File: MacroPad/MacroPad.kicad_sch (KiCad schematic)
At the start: 26 parts, among them SW1 CherryMX, SW10 CherryMX, SW12 CherryMX, SW2 CherryMX, SW3 CherryMX, SW4 CherryMX, SW5 CherryMX, SW6 CherryMX, SW7 CherryMX, SW8 CherryMX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

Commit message: updated materials list
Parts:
- added O1: SSD1306, Connector_PinSocket_2.54mm:PinSocket_1x04_P2.54mm_Vertical, symbol Connector:Conn_01x04_Male
- added SW11: CherryMX, Switch_Keyboard_Cherry_MX:SW_Cherry_MX_Plate_1.00u, symbol CherryMX:CherryMX
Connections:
- net GND: now also O1.4 (Pin_4), SW11.2
- net SW1: now also U1.25 (*GPIO0/BOOT/ADC2_CH1); no longer U1.7 (32K_XP/GPIO32/ADC1_CH4)
- net SW10: now also U1.28 (GPIO17); no longer U1.10 (DAC_2/ADC2_CH9/GPIO26)
- net SW11: now also U1.29 (*GPIO5), SW11.1; no longer U1.11 (ADC2_CH7/GPIO27)
- net SW12: now also U1.12 (MTMS/GPIO14/ADC2_CH6); no longer U1.36 (GPIO22)
- net SW2: now also U1.13 (*MTDI/GPIO12/ADC2_CH5); no longer U1.37 (GPIO23)
- net SW3: now also U1.9 (DAC_1/ADC2_CH8/GPIO25); no longer U1.30 (GPIO18)
- net SW4: now also U1.26 (ADC2_CH0/GPIO4); no longer U1.8 (32K_XN/GPIO33/ADC1_CH5)
- net SW5: now also U1.31 (GPIO19); no longer U1.13 (*MTDI/GPIO12/ADC2_CH5)
- net SW6: now also U1.10 (DAC_2/ADC2_CH9/GPIO26); no longer U1.31 (GPIO19)
- net SW7: now also U1.27 (GPIO16); no longer U1.9 (DAC_1/ADC2_CH8/GPIO25)
- net SW8: now also U1.30 (GPIO18); no longer U1.12 (MTMS/GPIO14/ADC2_CH6)
- net SW9: now also U1.11 (ADC2_CH7/GPIO27); no longer U1.33 (GPIO21)
- net at C1.1, D1.1 (VDD), D10.1 (VDD)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: now also O1.3 (Pin_3)
- new net: O1.1 (Pin_1), U1.33 (GPIO21)
- new net: O1.2 (Pin_2), U1.36 (GPIO22)
- no-connect marks 23 -> 21

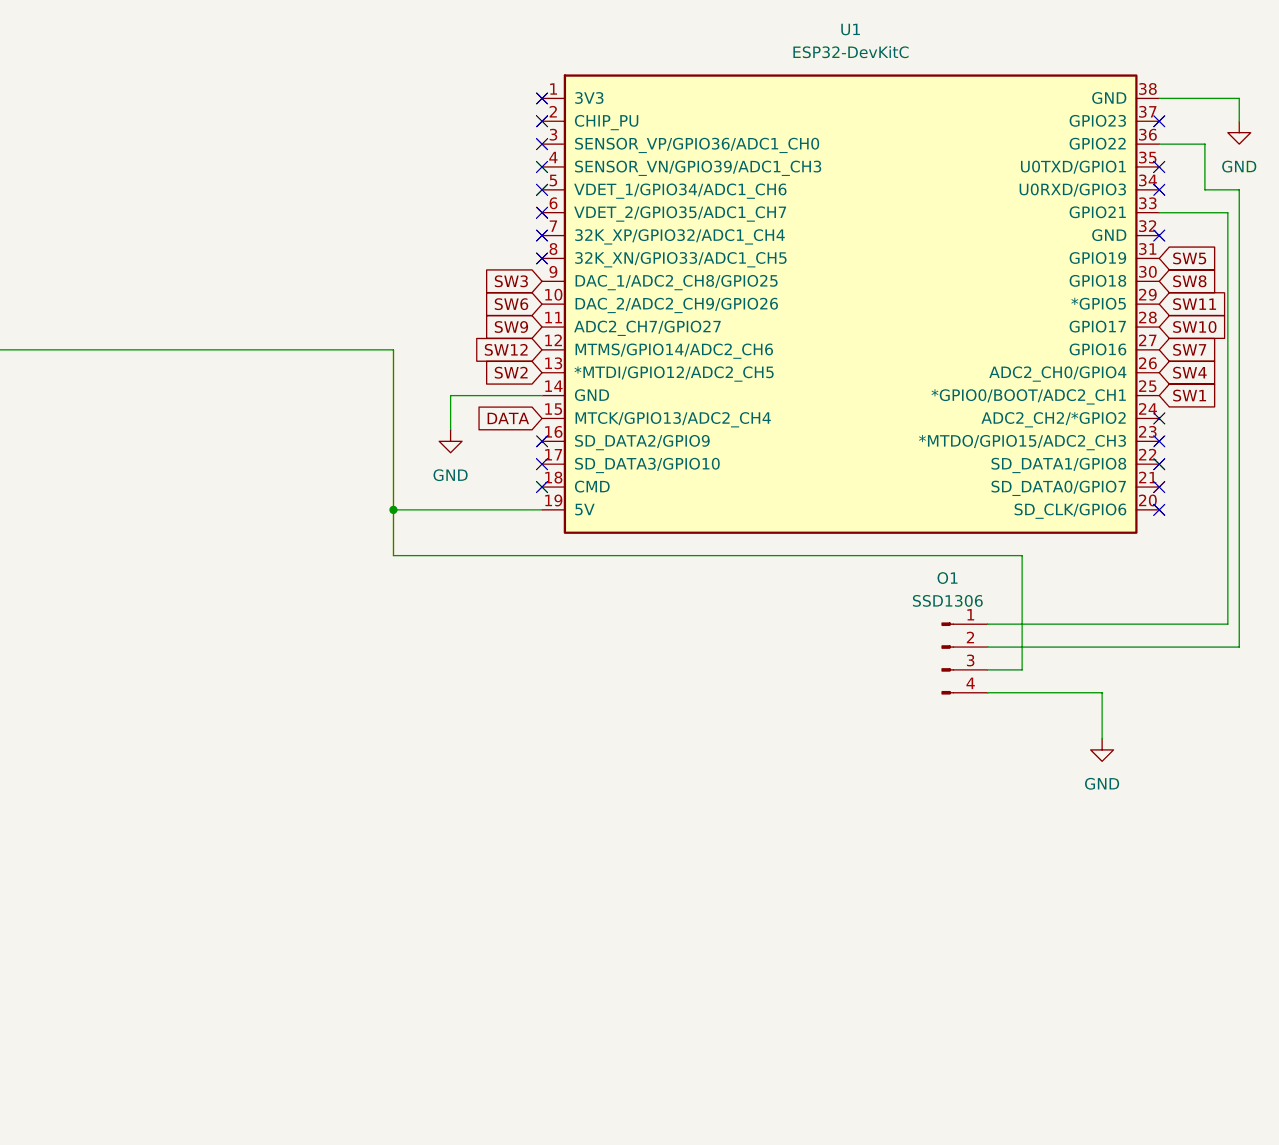
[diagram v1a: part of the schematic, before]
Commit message: redesign, added buttons and rotary encoder
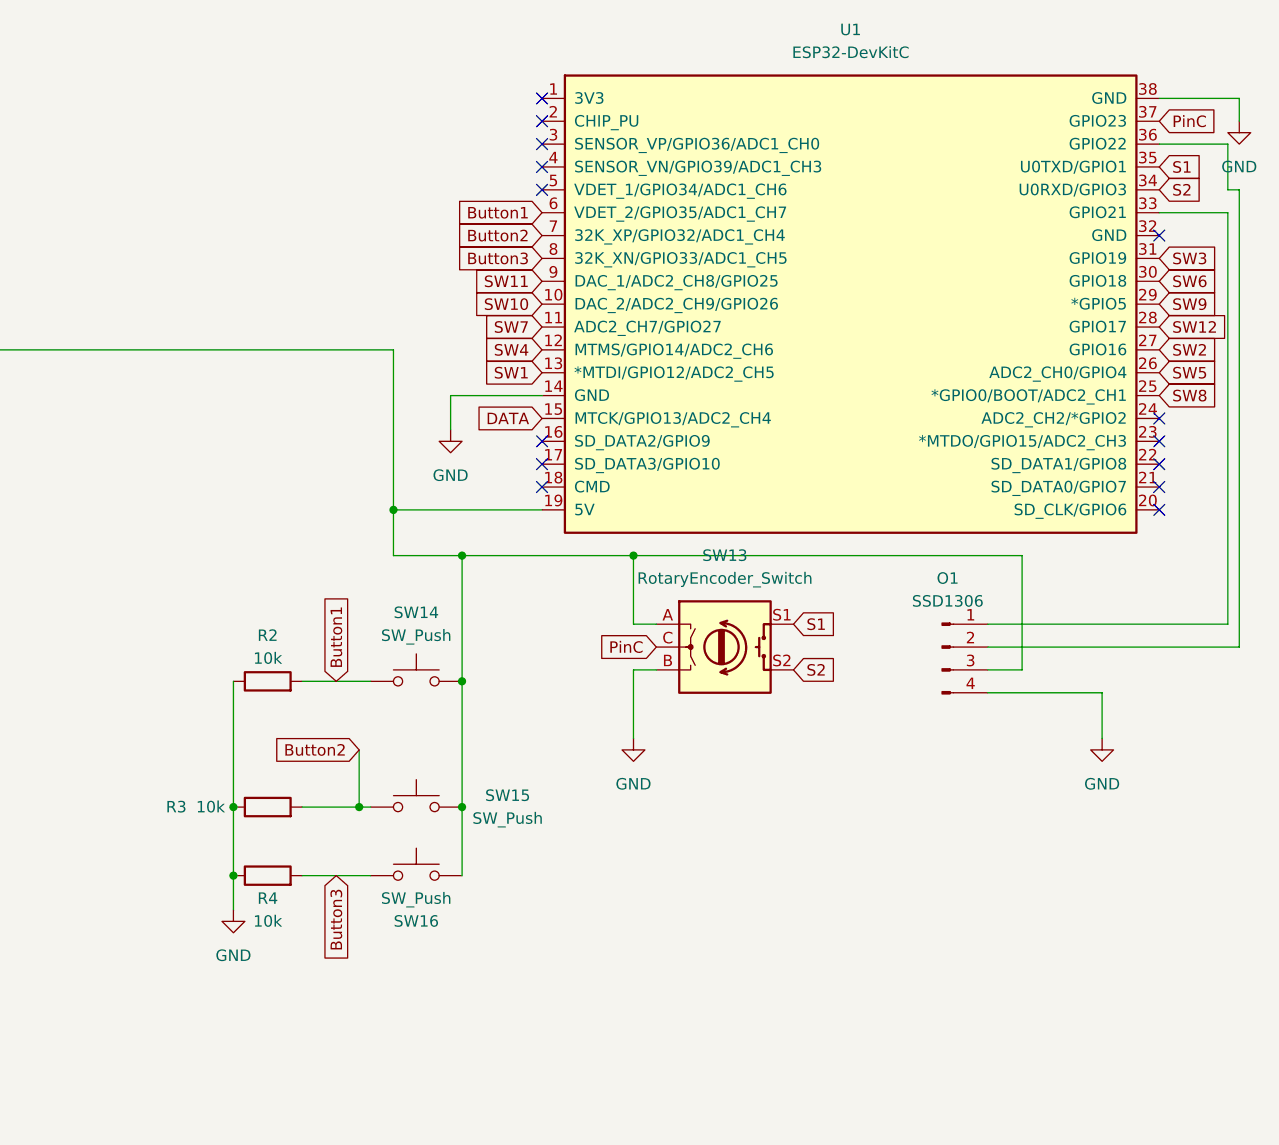
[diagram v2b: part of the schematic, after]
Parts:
- added R2, R3, R4: 10k, Resistor_SMD:R_1206_3216Metric_Pad1.30x1.75mm_HandSolder, symbol Device:R
- added SW13: RotaryEncoder_Switch, Rotary_Encoder:RotaryEncoder_Alps_EC12E-Switch_Vertical_H20mm_CircularMountingHoles, symbol Device:RotaryEncoder_Switch
- added SW14, SW15, SW16: SW_Push, Button_Switch_THT:SW_PUSH_6mm, symbol Switch:SW_Push
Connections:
- net GND: now also R2.1, R3.1, R4.1, SW13.B
- net SW1: now also U1.13 (*MTDI/GPIO12/ADC2_CH5); no longer U1.25 (*GPIO0/BOOT/ADC2_CH1)
- net SW10: now also U1.10 (DAC_2/ADC2_CH9/GPIO26); no longer U1.28 (GPIO17)
- net SW11: now also U1.9 (DAC_1/ADC2_CH8/GPIO25); no longer U1.29 (*GPIO5)
- net SW12: now also U1.28 (GPIO17); no longer U1.12 (MTMS/GPIO14/ADC2_CH6)
- net SW2: now also U1.27 (GPIO16); no longer U1.13 (*MTDI/GPIO12/ADC2_CH5)
- net SW3: now also U1.31 (GPIO19); no longer U1.9 (DAC_1/ADC2_CH8/GPIO25)
- net SW4: now also U1.12 (MTMS/GPIO14/ADC2_CH6); no longer U1.26 (ADC2_CH0/GPIO4)
- net SW5: now also U1.26 (ADC2_CH0/GPIO4); no longer U1.31 (GPIO19)
- net SW6: now also U1.30 (GPIO18); no longer U1.10 (DAC_2/ADC2_CH9/GPIO26)
- net SW7: now also U1.11 (ADC2_CH7/GPIO27); no longer U1.27 (GPIO16)
- net SW8: now also U1.25 (*GPIO0/BOOT/ADC2_CH1); no longer U1.30 (GPIO18)
- net SW9: now also U1.29 (*GPIO5); no longer U1.11 (ADC2_CH7/GPIO27)
- net at C1.1, D1.1 (VDD), D10.1 (VDD)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: now also SW13.A, SW14.2, SW15.2, SW16.2
- net S2: now reaches U1.34 (U0RXD/GPIO3)
- net S2: now also SW13.S2
- net S1: now reaches U1.35 (U0TXD/GPIO1)
- net S1: now also SW13.S1
- net PinC: now reaches U1.37 (GPIO23)
- net PinC: now also SW13.C
- net Button1: now reaches U1.6 (VDET_2/GPIO35/ADC1_CH7)
- net Button1: now also R2.2, SW14.1
- net Button2: now reaches U1.7 (32K_XP/GPIO32/ADC1_CH4)
- net Button2: now also R3.2, SW15.1
- net Button3: now reaches U1.8 (32K_XN/GPIO33/ADC1_CH5)
- net Button3: now also R4.2, SW16.1
- no-connect marks 21 -> 15
